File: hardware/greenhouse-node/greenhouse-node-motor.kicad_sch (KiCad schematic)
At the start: 29 parts

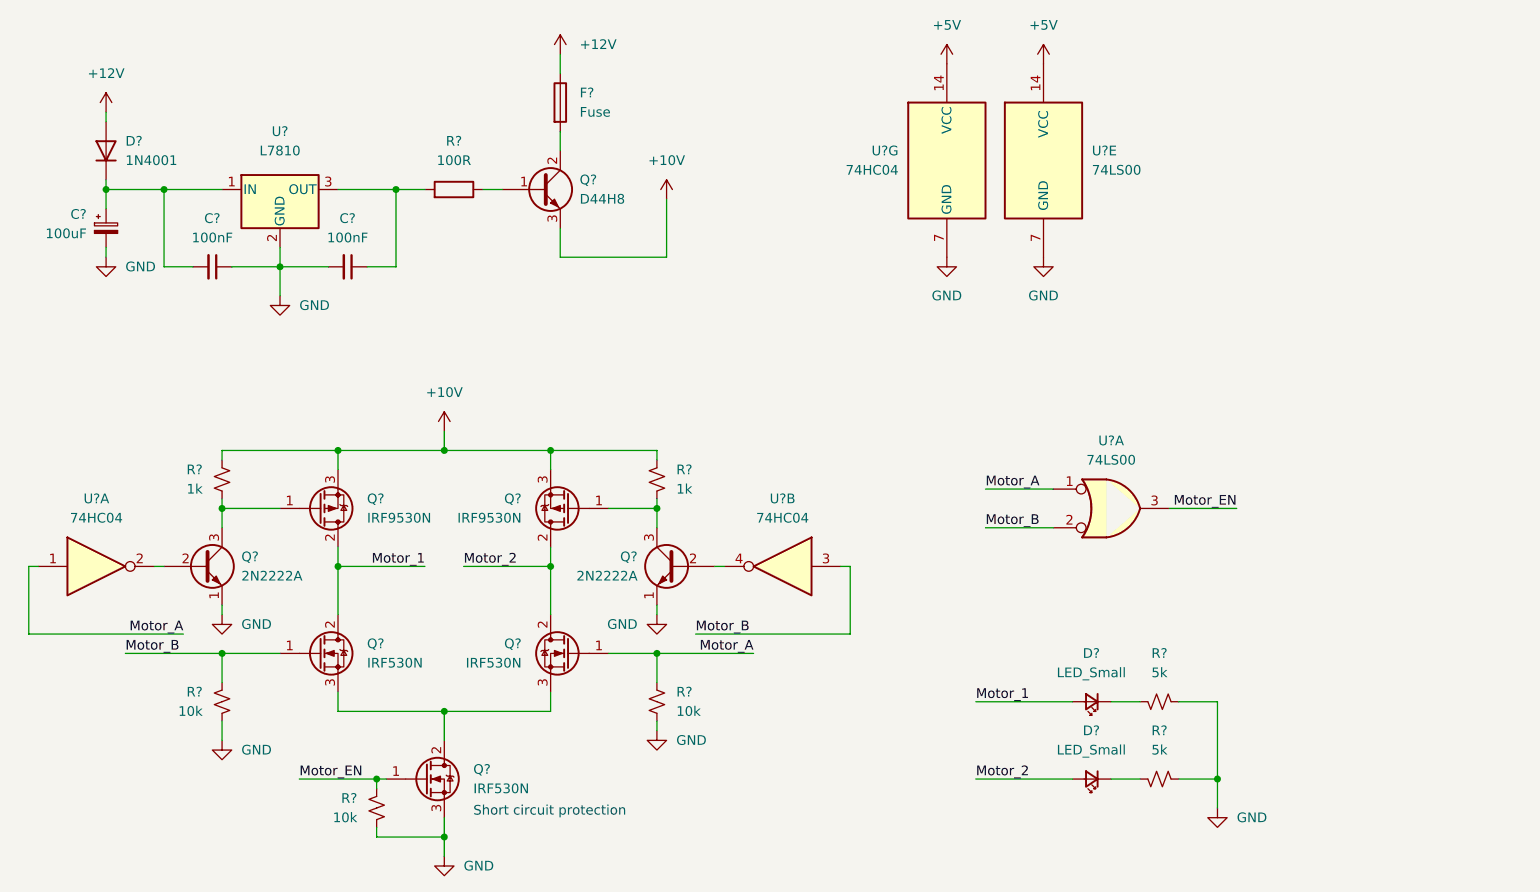
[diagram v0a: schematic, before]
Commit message: Redesigned H-bridge
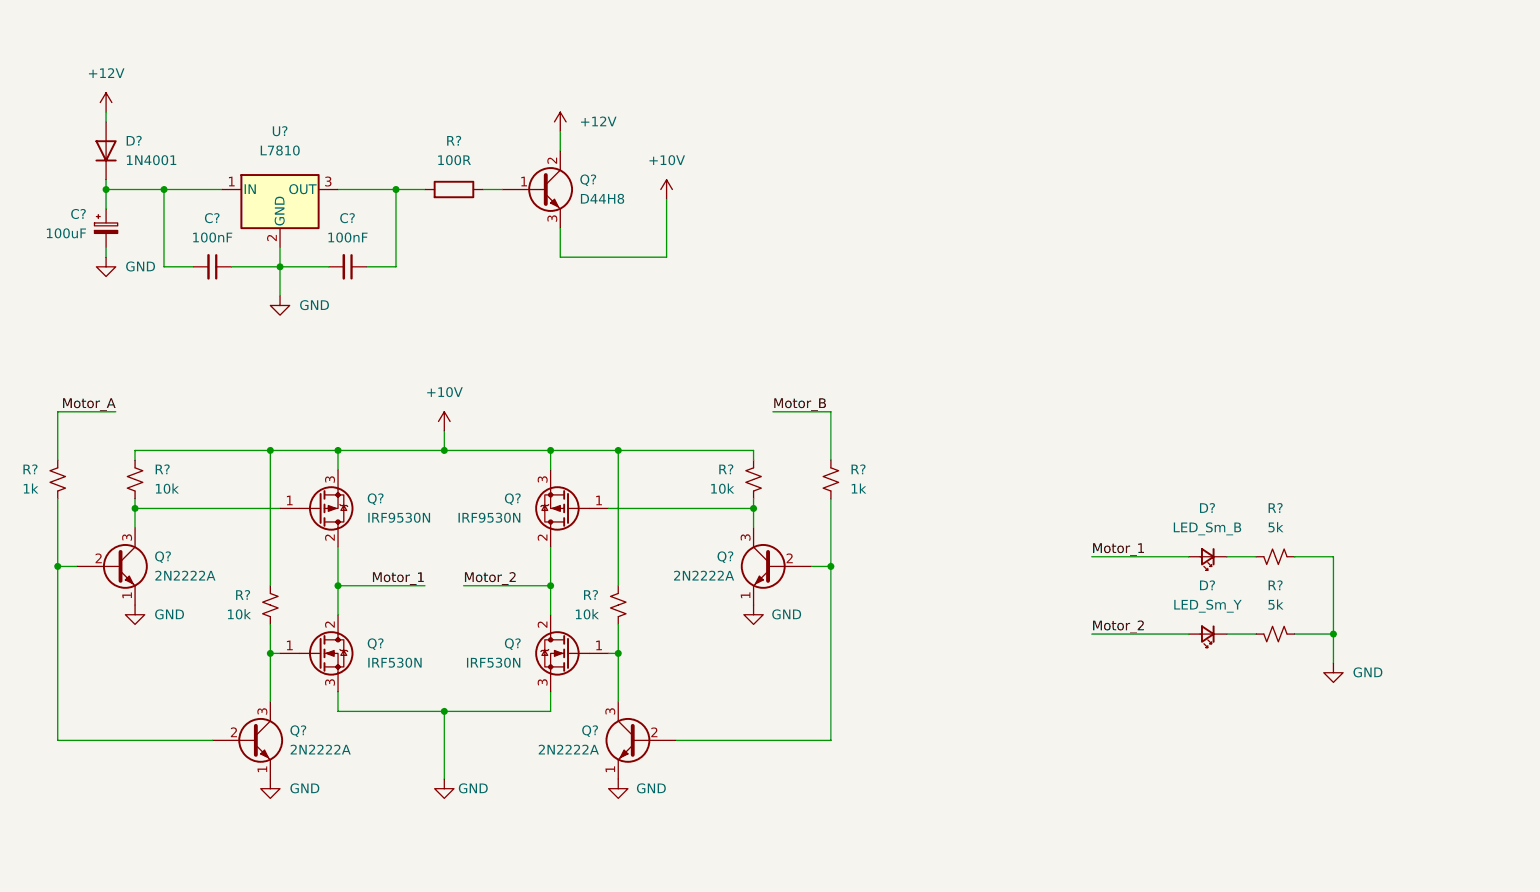
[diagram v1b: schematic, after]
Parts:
- removed F?: Fuse, symbol Device:Fuse
- removed Q?: 2N2222A, Package_TO_SOT_THT:TO-92_Inline, symbol Nick:2N2222A
- removed Q?: IRF530N, Package_TO_SOT_THT:TO-220-3_Vertical, symbol Transistor_FET:IRF540N
- removed R? (x2): 1k, symbol Device:R_Small_US
- removed R? (x3): 10k, symbol Device:R_Small_US
- removed U? (x3): 74HC04, symbol 74xx:74HC04
- removed U? (x2): 74LS00, symbol 74xx:74LS00
- added Q? (x3): 2N2222A, Package_TO_SOT_THT:TO-92_Inline, symbol Nick:2N2222A
- added R? (x2): 1k, symbol Device:R_Small_US
- added R? (x4): 10k, symbol Device:R_Small_US
- D?: value LED_Small -> LED_Sm_B
- D?: value LED_Small -> LED_Sm_Y
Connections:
- net +10V: now also R?.2, R?.2, R?.2, R?.2
- net +12V: now also Q?.2 (C)
- net GND: now also Q?.3 (S), Q?.3 (S), Q?.1 (E), Q?.1 (E), Q?.1 (E)
- net Motor_A: now also R?.2; no longer Q?.1 (G)
- net Motor_B: now also R?.2; no longer Q?.1 (G)
- net at Q?.1 (G), Q?.3 (C): now also R?.1
- net at Q?.1 (G): now also Q?.3 (C), R?.1
- net at Q?.2 (B): now also Q?.2 (B), R?.1
- new net: Q?.1 (G), Q?.3 (C), R?.1 (x2)
- new net: Q?.2 (B), Q?.2 (B), R?.1
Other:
- note removed: "Short circuit protection"
- moved on the sheet: D?, Q?, R?

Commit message: First PCB design for node
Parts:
- removed C?: 100uF, symbol Device:C_Polarized_Small
- removed D?: 1N4001, Diode_THT:D_DO-41_SOD81_P10.16mm_Horizontal, symbol Diode:1N4001
- added J6: Conn_01x02_Male, Connector_Molex:Molex_KK-396_A-41791-0002_1x02_P3.96mm_Vertical, symbol Connector:Conn_01x02_Male
- C5: renamed from C?; value 100nF -> 330nF
- D5, D6: renamed from D?; footprint (none) -> LED_THT:LED_D3.0mm
- Q4, Q5, Q6, Q7, Q8: renamed from Q?; footprint Package_TO_SOT_THT:TO-220-3_Vertical -> Package_TO_SOT_THT:TO-220-3_Horizontal_TabDown
- R10, R11, R12, R13, R5, R6, R7, R9: renamed from R?; footprint (none) -> Resistor_THT:R_Axial_DIN0204_L3.6mm_D1.6mm_P7.62mm_Horizontal
- gave numbers to parts that had none: 7
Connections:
- net +12V: now also C5.2, U4.1 (IN)
- net Motor_1: now also J6.1 (Pin_1)
- net Motor_2: now also J6.2 (Pin_2)
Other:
- moved on the sheet: C5, C6, D5, D6, Q10, Q2, Q3, Q4, Q5, Q6, Q7, Q8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

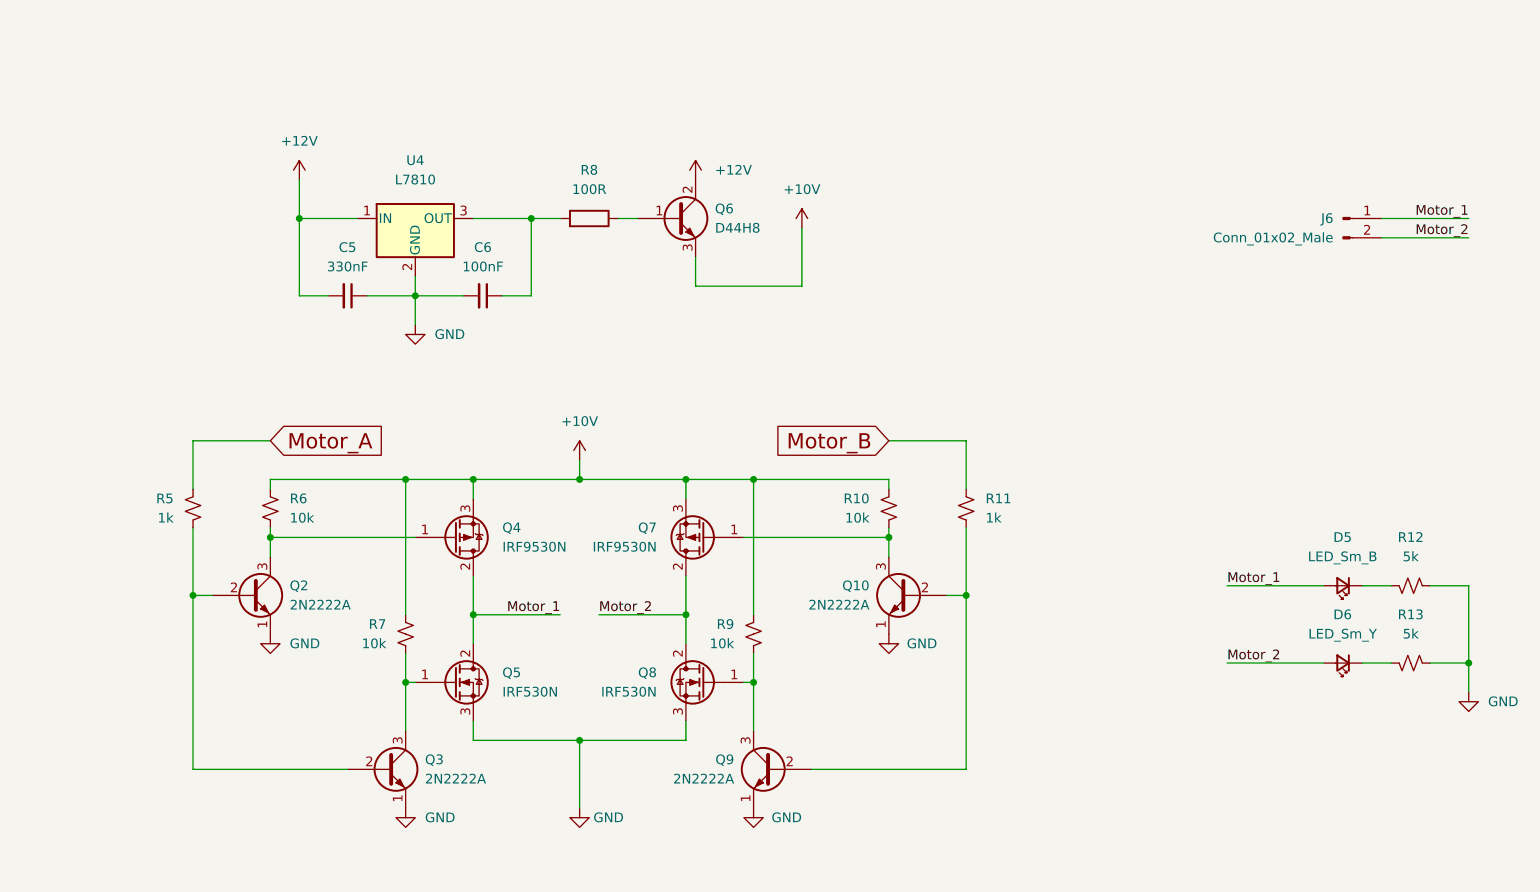
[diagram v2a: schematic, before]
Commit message: Redesign node PCB around mounting holes
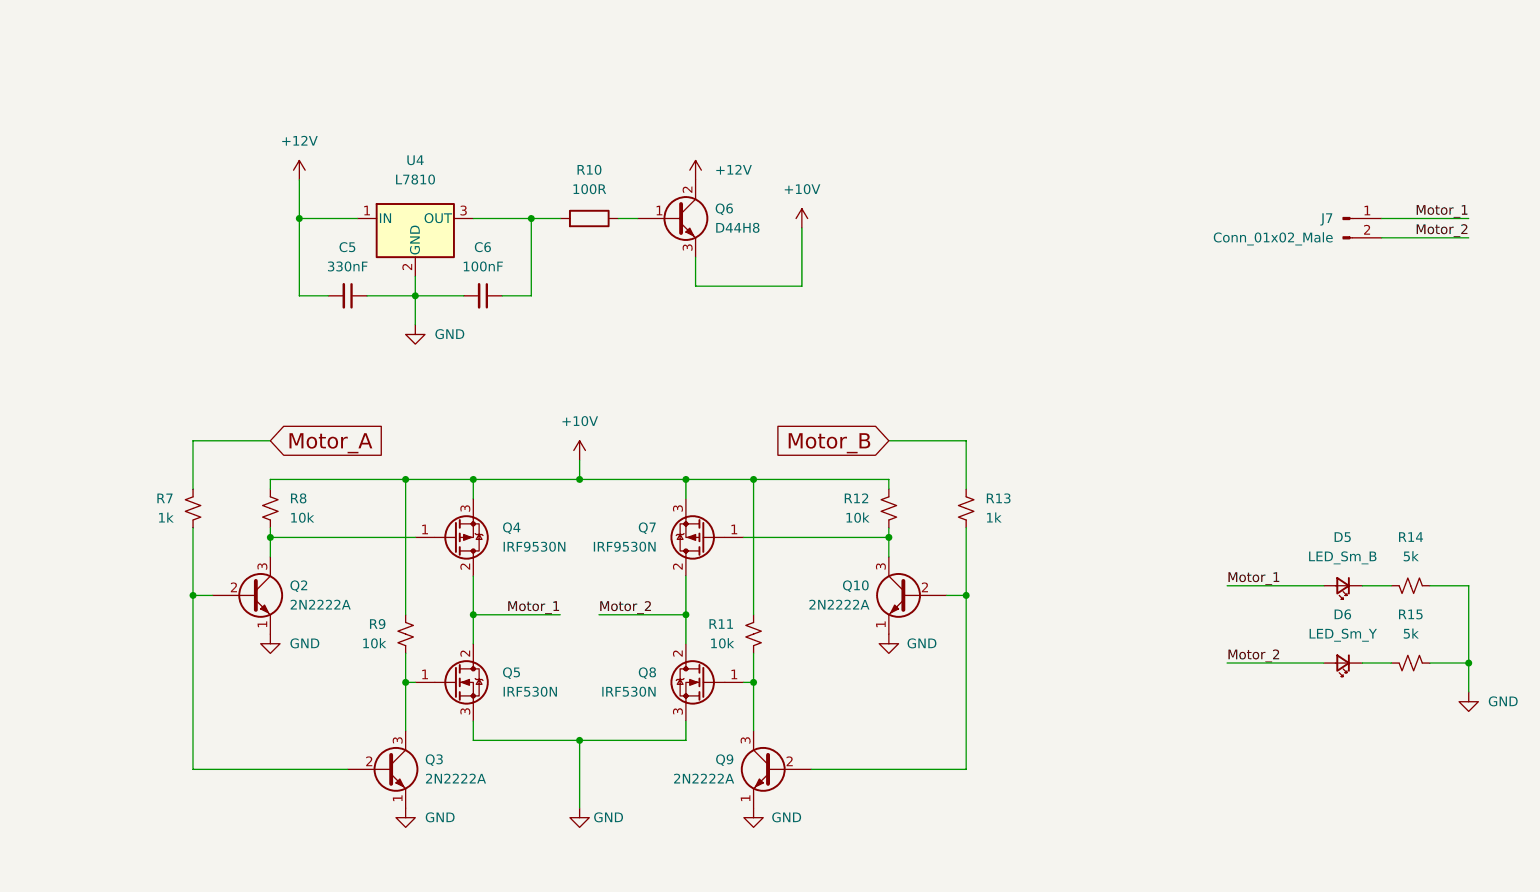
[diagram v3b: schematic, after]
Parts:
- renumbered J6 to J7, R8 to R10, R9 to R11, R10 to R12, R11 to R13, R12 to R14, R13 to R15, R5 to R7, R6 to R8, R7 to R9
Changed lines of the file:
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@@
   (symbol (lib_id "power:+12V") (at 127 53.34 0) (unit 1)
     (in_bom yes) (on_board yes) (fields_autoplaced)
-    (property "Reference" "#PWR025" (id 0) (at 127 57.15 0)
+    (property "Reference" "#PWR026" (id 0) (at 127 57.15 0)
       (effects (font (size 1.27 1.27)) hide)
     )
@@
   (symbol (lib_id "Device:R_Small_US") (at 60.96 96.52 0) (mirror x) (unit 1)
     (in_bom yes) (on_board yes) (fields_autoplaced)
-    (property "Reference" "R5" (id 0) (at 58.42 95.2499 0)
+    (property "Reference" "R7" (id 0) (at 58.42 95.2499 0)
       (effects (font (size 1.27 1.27)) (justify right))
     )
@@
   (symbol (lib_id "power:GND") (at 228.6 120.65 0) (unit 1)
     (in_bom yes) (on_board yes) (fields_autoplaced)
-    (property "Reference" "#PWR029" (id 0) (at 228.6 127 0)
+    (property "Reference" "#PWR030" (id 0) (at 228.6 127 0)
       (effects (font (size 1.27 1.27)) hide)
     )
@@
   (symbol (lib_id "Device:R_Small_US") (at 134.62 113.03 0) (mirror x) (unit 1)
     (in_bom yes) (on_board yes) (fields_autoplaced)
-    (property "Reference" "R9" (id 0) (at 132.08 111.7599 0)
+    (property "Reference" "R11" (id 0) (at 132.08 111.7599 0)
       (effects (font (size 1.27 1.27)) (justify right))
     )
@@
   (symbol (lib_id "power:GND") (at 90.17 72.39 0) (unit 1)
     (in_bom yes) (on_board yes) (fields_autoplaced)
-    (property "Reference" "#PWR022" (id 0) (at 90.17 78.74 0)
+    (property "Reference" "#PWR023" (id 0) (at 90.17 78.74 0)
       (effects (font (size 1.27 1.27)) hide)
     )
@@
   (symbol (lib_id "power:+12V") (at 74.93 53.34 0) (unit 1)
     (in_bom yes) (on_board yes) (fields_autoplaced)
-    (property "Reference" "#PWR020" (id 0) (at 74.93 57.15 0)
+    (property "Reference" "#PWR021" (id 0) (at 74.93 57.15 0)
       (effects (font (size 1.27 1.27)) hide)
     )
@@
   (symbol (lib_id "power:+10V") (at 111.76 90.17 0) (unit 1)
     (in_bom yes) (on_board yes) (fields_autoplaced)
-    (property "Reference" "#PWR023" (id 0) (at 111.76 93.98 0)
+    (property "Reference" "#PWR024" (id 0) (at 111.76 93.98 0)
       (effects (font (size 1.27 1.27)) hide)
     )
@@
   (symbol (lib_id "Device:R_Small_US") (at 152.4 96.52 0) (mirror x) (unit 1)
     (in_bom yes) (on_board yes) (fields_autoplaced)
-    (property "Reference" "R10" (id 0) (at 149.86 95.2499 0)
+    (property "Reference" "R12" (id 0) (at 149.86 95.2499 0)
       (effects (font (size 1.27 1.27)) (justify right))
     )
@@
   (symbol (lib_id "Device:R_Small_US") (at 71.12 96.52 180) (unit 1)
     (in_bom yes) (on_board yes) (fields_autoplaced)
-    (property "Reference" "R6" (id 0) (at 73.66 95.2499 0)
+    (property "Reference" "R8" (id 0) (at 73.66 95.2499 0)
       (effects (font (size 1.27 1.27)) (justify right))
     )
@@
   (symbol (lib_id "power:GND") (at 152.4 113.03 0) (mirror y) (unit 1)
     (in_bom yes) (on_board yes)
-    (property "Reference" "#PWR028" (id 0) (at 152.4 119.38 0)
+    (property "Reference" "#PWR029" (id 0) (at 152.4 119.38 0)
       (effects (font (size 1.27 1.27)) hide)
     )
@@
   (symbol (lib_id "power:+10V") (at 140.97 59.69 0) (unit 1)
     (in_bom yes) (on_board yes) (fields_autoplaced)
-    (property "Reference" "#PWR027" (id 0) (at 140.97 63.5 0)
+    (property "Reference" "#PWR028" (id 0) (at 140.97 63.5 0)
       (effects (font (size 1.27 1.27)) hide)
     )
@@
   (symbol (lib_id "Connector:Conn_01x02_Male") (at 212.09 58.42 0) (unit 1)
     (in_bom yes) (on_board yes) (fields_autoplaced)
-    (property "Reference" "J6" (id 0) (at 210.82 58.4199 0)
+    (property "Reference" "J7" (id 0) (at 210.82 58.4199 0)
       (effects (font (size 1.27 1.27)) (justify right))
     )
@@
   (symbol (lib_id "power:GND") (at 134.62 135.89 0) (mirror y) (unit 1)
     (in_bom yes) (on_board yes)
-    (property "Reference" "#PWR026" (id 0) (at 134.62 142.24 0)
+    (property "Reference" "#PWR027" (id 0) (at 134.62 142.24 0)
       (effects (font (size 1.27 1.27)) hide)
     )
@@
   (symbol (lib_id "Device:R") (at 113.03 58.42 270) (mirror x) (unit 1)
     (in_bom yes) (on_board yes) (fields_autoplaced)
-    (property "Reference" "R8" (id 0) (at 113.03 52.07 90))
+    (property "Reference" "R10" (id 0) (at 113.03 52.07 90))
     (property "Value" "100R" (id 1) (at 113.03 54.61 90))
     (property "Footprint" "Resistor_THT:R_Axial_DIN0204_L3.6mm_D1.6mm_P5.08mm_Horizontal" (id 2) (at 113.03 60.198 90)
@@
   (symbol (lib_id "power:GND") (at 88.9 135.89 0) (unit 1)
     (in_bom yes) (on_board yes) (fields_autoplaced)
-    (property "Reference" "#PWR021" (id 0) (at 88.9 142.24 0)
+    (property "Reference" "#PWR022" (id 0) (at 88.9 142.24 0)
       (effects (font (size 1.27 1.27)) hide)
     )
@@
   (symbol (lib_id "Device:R_Small_US") (at 162.56 96.52 180) (unit 1)
     (in_bom yes) (on_board yes) (fields_autoplaced)
-    (property "Reference" "R11" (id 0) (at 165.1 95.2499 0)
+    (property "Reference" "R13" (id 0) (at 165.1 95.2499 0)
       (effects (font (size 1.27 1.27)) (justify right))
     )
@@
   (symbol (lib_id "Device:R_Small_US") (at 88.9 113.03 180) (unit 1)
     (in_bom yes) (on_board yes) (fields_autoplaced)
-    (property "Reference" "R7" (id 0) (at 86.36 111.7599 0)
+    (property "Reference" "R9" (id 0) (at 86.36 111.7599 0)
       (effects (font (size 1.27 1.27)) (justify left))
     )
@@
   (symbol (lib_id "Device:R_Small_US") (at 220.98 116.84 270) (mirror x) (unit 1)
     (in_bom yes) (on_board yes) (fields_autoplaced)
-    (property "Reference" "R13" (id 0) (at 220.98 110.49 90))
+    (property "Reference" "R15" (id 0) (at 220.98 110.49 90))
     (property "Value" "5k" (id 1) (at 220.98 113.03 90))
     (property "Footprint" "Resistor_THT:R_Axial_DIN0204_L3.6mm_D1.6mm_P7.62mm_Horizontal" (id 2) (at 220.98 116.84 0)
@@
   (symbol (lib_id "Device:R_Small_US") (at 220.98 106.68 270) (mirror x) (unit 1)
     (in_bom yes) (on_board yes) (fields_autoplaced)
-    (property "Reference" "R12" (id 0) (at 220.98 100.33 90))
+    (property "Reference" "R14" (id 0) (at 220.98 100.33 90))
     (property "Value" "5k" (id 1) (at 220.98 102.87 90))
     (property "Footprint" "Resistor_THT:R_Axial_DIN0204_L3.6mm_D1.6mm_P7.62mm_Horizontal" (id 2) (at 220.98 106.68 0)
@@
   (symbol (lib_id "power:GND") (at 111.76 135.89 0) (unit 1)
     (in_bom yes) (on_board yes)
-    (property "Reference" "#PWR024" (id 0) (at 111.76 142.24 0)
+    (property "Reference" "#PWR025" (id 0) (at 111.76 142.24 0)
       (effects (font (size 1.27 1.27)) hide)
     )
@@
   (symbol (lib_id "power:GND") (at 71.12 113.03 0) (unit 1)
     (in_bom yes) (on_board yes) (fields_autoplaced)
-    (property "Reference" "#PWR019" (id 0) (at 71.12 119.38 0)
-      (effects (font (size 1.27 1.27)) hide)
-    )
+    (property "Reference" "#PWR020" (id 0) (at 71.12 119.38 0)
+      (effects (font (size 1.27 1.27)) hide)
+    )
